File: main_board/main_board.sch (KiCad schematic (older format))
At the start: 132 parts, among them J1 stepper 0, J10 24VDCout5, J11 5VDCout0, J12 5VDCout1, J13 5VDCout2, J14 5VDCout3, J15 5VDCout4, J16 5VDCout5, J17 temperature measure 0, J18 temperature measure 1, J19 I2C, J2 stepper 1, J20 I2C, J21 I2C, J22 I2C, J23 hall measure 0, J24 weight measure 0, J25 light measure 0, J26 24VDC_in, J27 24VDC to 5VDC step down, J28 24VDC, J29 24VDC, J3 stepper 2, J30 24VDC, J31 5VDC, J32 5VDC, J33 5VDC, J34 hall measure 1, J35 reflective sensor 0, J36 24VDC, J37 24VDC, J38 24VDC, J39 5VDC, J4 stepper 3, J40 5VDC, J41 5VDC, J42 Conn_01x05_Male, J5 24VDCout0, J6 24VDCout1, J7 24VDCout2, J8 24VDCout3, J9 24VDCout4, Q1 Q_NMOS_GDS, Q10 BS170, Q11 BS170, Q12 BS170, Q2 Q_NMOS_GDS, Q3 Q_NMOS_GDS, Q4 Q_NMOS_GDS, Q5 Q_NMOS_GDS, Q6 Q_NMOS_GDS, Q7 BS170, Q8 BS170, Q9 BS170, U1 ESP32-DEVKITC-32D, U2 PCA9685PW

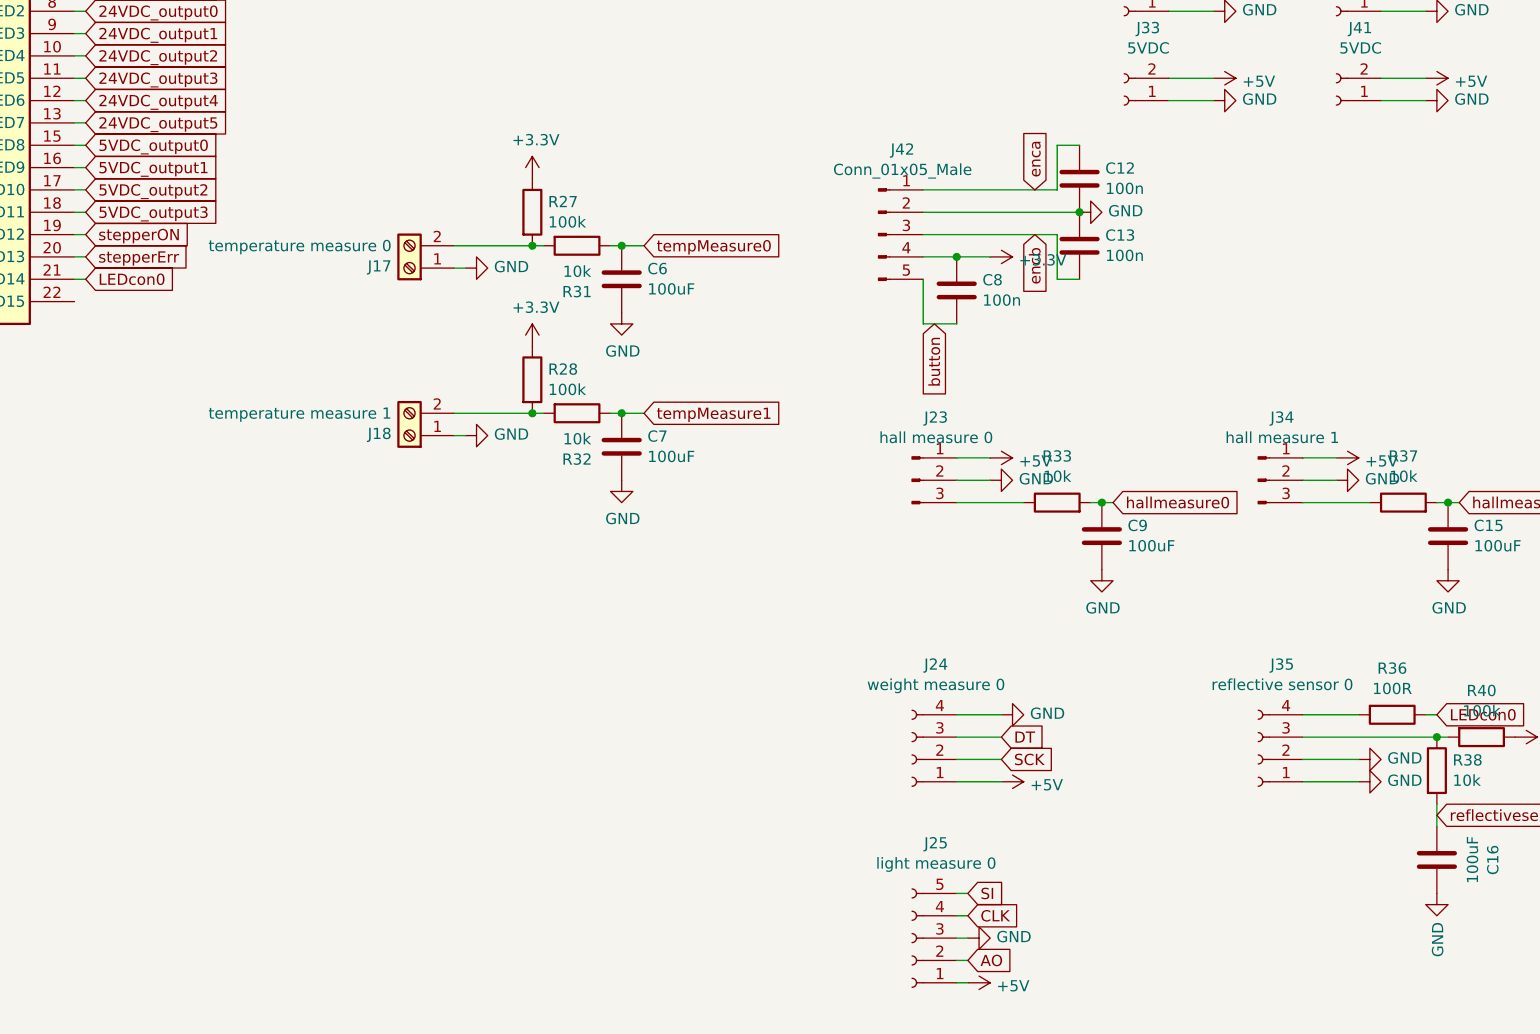
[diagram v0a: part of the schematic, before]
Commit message: added gnd zones
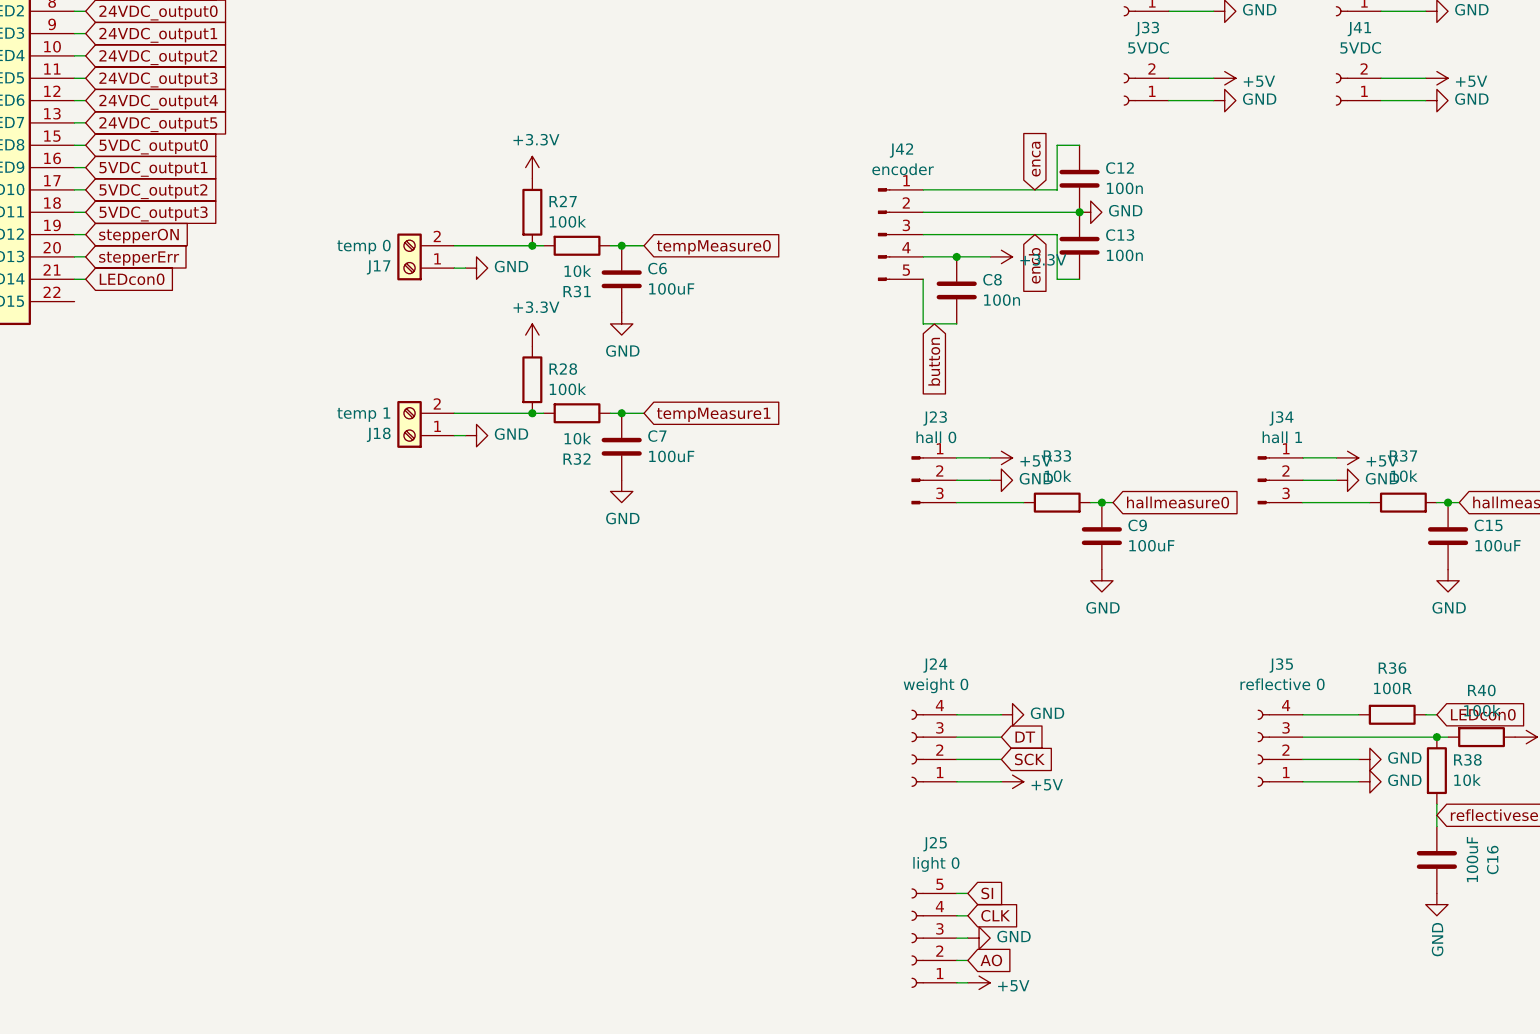
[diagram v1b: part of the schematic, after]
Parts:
- J17: value temperature measure 0 -> temp 0
- J18: value temperature measure 1 -> temp 1
- J23: value hall measure 0 -> hall 0
- J24: value weight measure 0 -> weight 0
- J25: value light measure 0 -> light 0
- J34: value hall measure 1 -> hall 1
- J35: value reflective sensor 0 -> reflective 0
- J42: value Conn_01x05_Male -> encoder

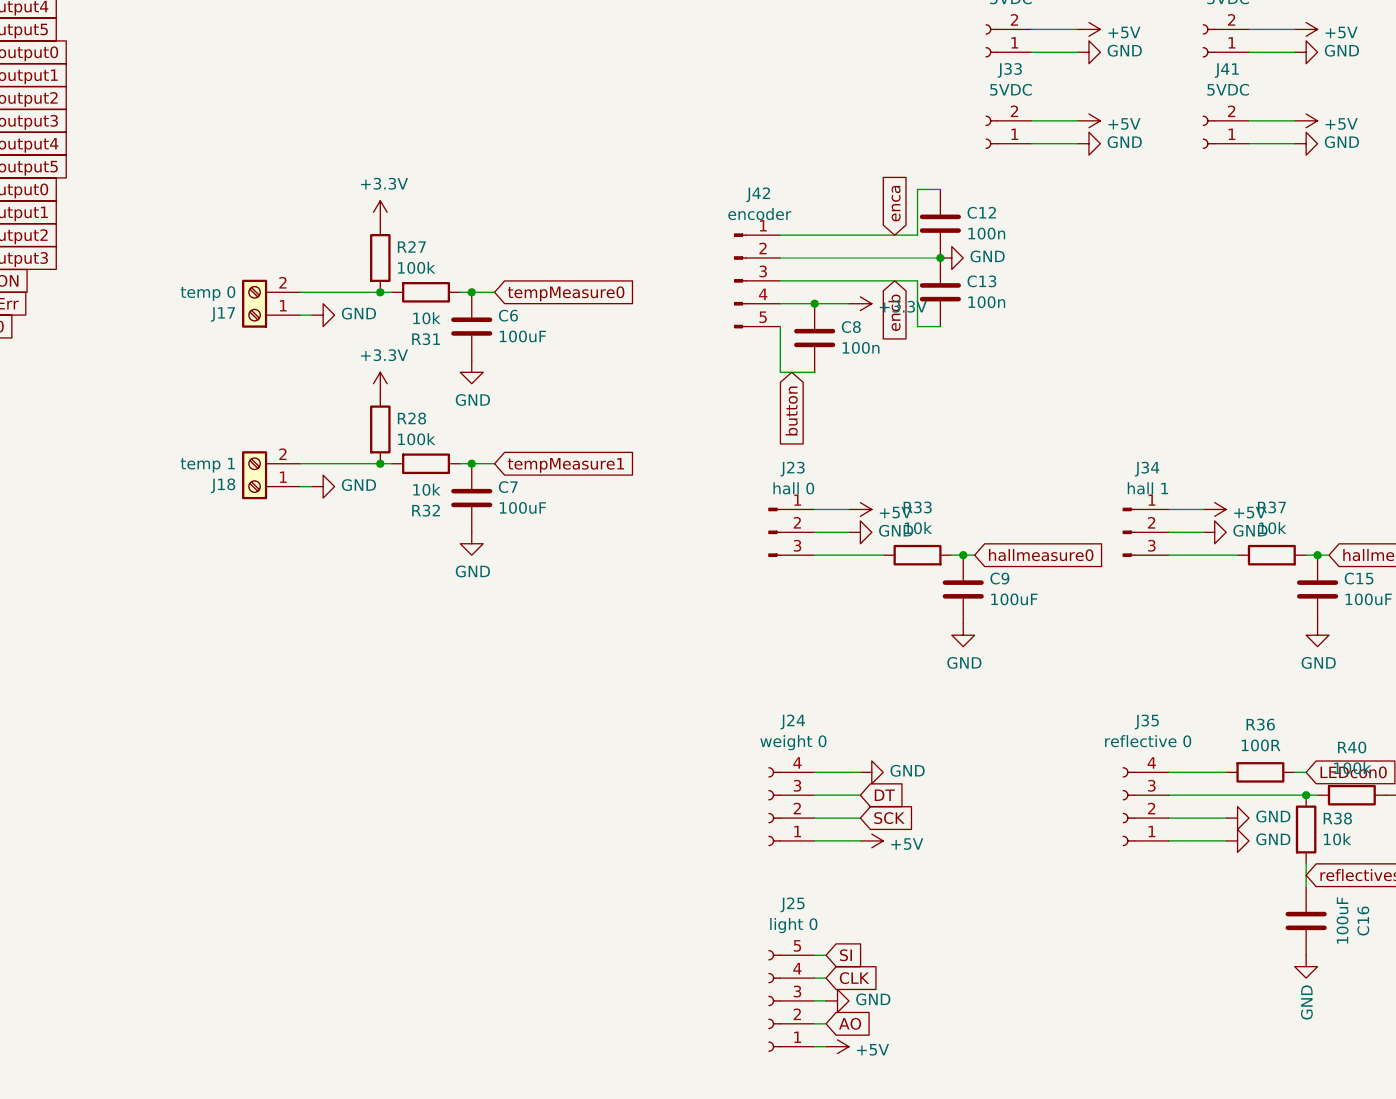
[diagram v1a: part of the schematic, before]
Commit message: part numbers added
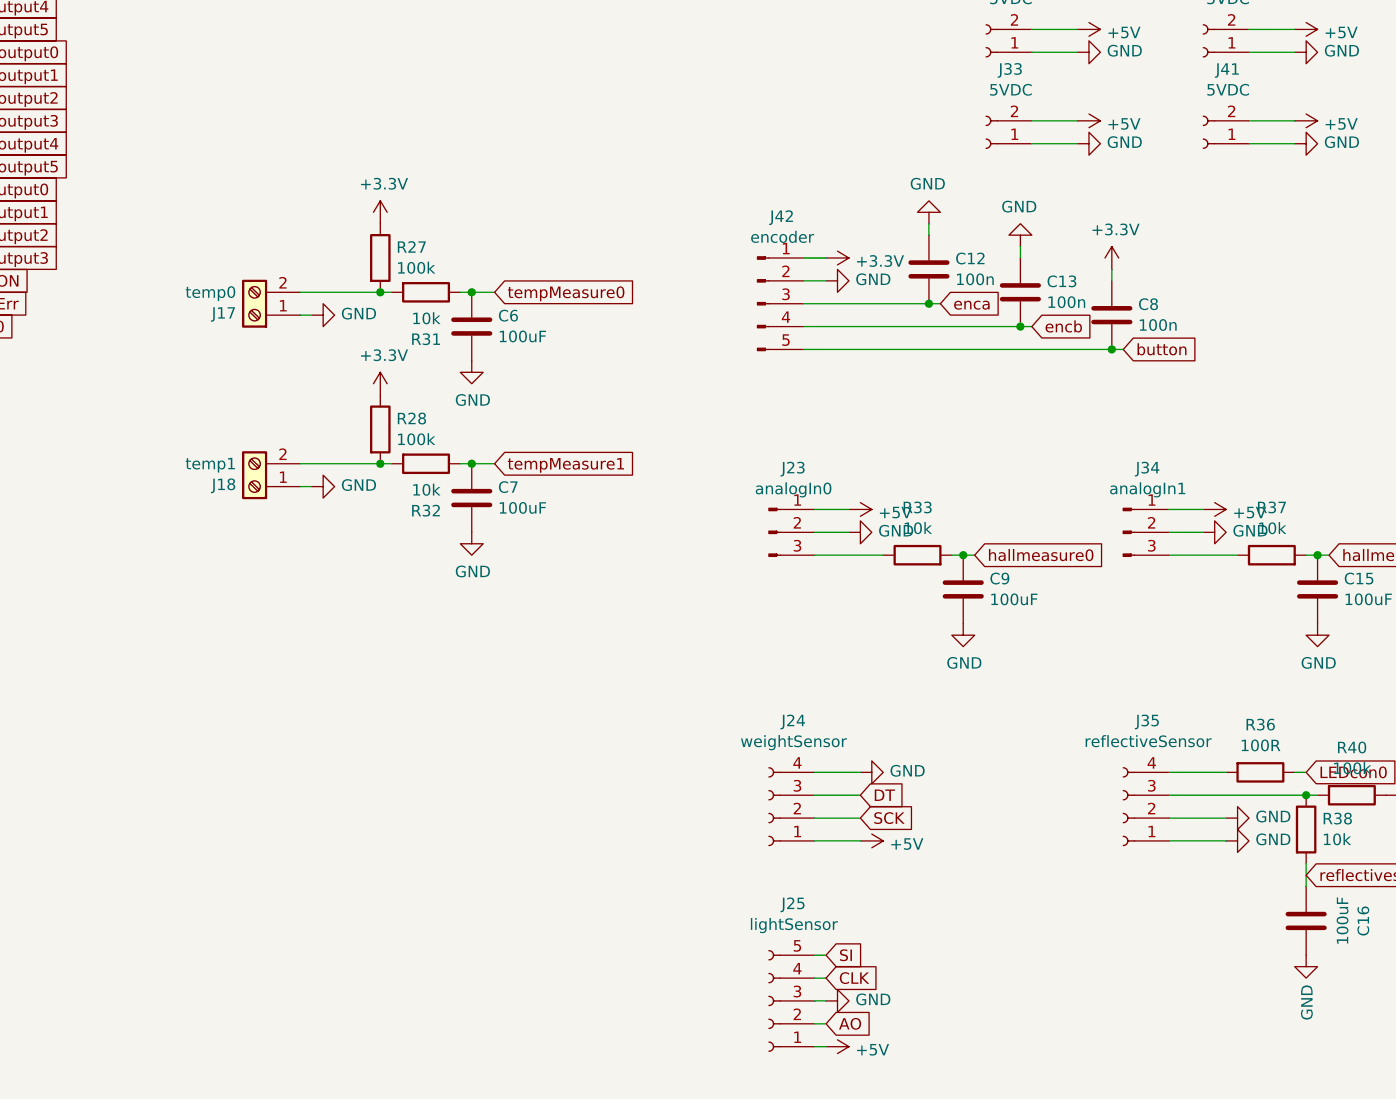
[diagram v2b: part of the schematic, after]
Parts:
- J17: value temp 0 -> temp0
- J18: value temp 1 -> temp1
- J23: value hall 0 -> analogIn0
- J24: value weight 0 -> weightSensor
- J25: value light 0 -> lightSensor
- J34: value hall 1 -> analogIn1
- J35: value reflective 0 -> reflectiveSensor
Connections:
- net +3V3: now also J42.1 (Pin_1); no longer J42.4 (Pin_4)
- net GND: now also C12.2; no longer C12.1
- net enca: now also C12.1, J42.3 (Pin_3); no longer C12.2, J42.1 (Pin_1)
- net encb: now also J42.4 (Pin_4); no longer J42.3 (Pin_3)
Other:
- moved on the sheet: C12, C13, C8, J42
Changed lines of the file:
@@
 Wire Wire Line
 	15000 2550 15200 2550
-Text GLabel 13450 4400 1    50   Input ~ 0
+Text GLabel 13650 4700 2    50   Input ~ 0
 enca
-Text GLabel 13450 4600 3    50   Input ~ 0
+Text GLabel 14050 4800 2    50   Input ~ 0
 encb
-Text GLabel 13000 5000 3    50   Input ~ 0
+Text GLabel 14450 4900 2    50   Input ~ 0
 button
 Text GLabel 9200 4100 2    50   Input ~ 0
@@
 P 12900 5700
 F 0 "J23" H 13008 5981 50  0000 C CNN
-F 1 "hall 0" H 13008 5890 50  0000 C CNN
+F 1 "analogIn0" H 13008 5890 50  0000 C CNN
 F 2 "Connector_PinHeader_2.54mm:PinHeader_1x03_P2.54mm_Vertical" H 12900 5700 50  0001 C CNN
 F 3 "~" H 12900 5700 50  0001 C CNN
@@
 L Device:C C8
 U 1 1 61B1A5D9
-P 13100 4850
-F 0 "C8" H 12985 4804 50  0000 R CNN
-F 1 "100n" H 12985 4895 50  0000 R CNN
-F 2 "Capacitor_SMD:C_0603_1608Metric_Pad1.08x0.95mm_HandSolder" H 13138 4700 50  0001 C CNN
-F 3 "~" H 13100 4850 50  0001 C CNN
-	1    13100 4850
+P 14400 4750
+F 0 "C8" H 14285 4704 50  0000 R CNN
+F 1 "100n" H 14285 4795 50  0000 R CNN
+F 2 "Capacitor_SMD:C_0603_1608Metric_Pad1.08x0.95mm_HandSolder" H 14438 4600 50  0001 C CNN
+F 3 "~" H 14400 4750 50  0001 C CNN
+	1    14400 4750
 	-1   0    0    1
 $EndComp
@@
 L Device:C C13
 U 1 1 61BB01E8
-P 13650 4650
-F 0 "C13" H 13535 4604 50  0000 R CNN
-F 1 "100n" H 13535 4695 50  0000 R CNN
-F 2 "Capacitor_SMD:C_0603_1608Metric_Pad1.08x0.95mm_HandSolder" H 13688 4500 50  0001 C CNN
-F 3 "~" H 13650 4650 50  0001 C CNN
-	1    13650 4650
+P 14000 4650
+F 0 "C13" H 13885 4604 50  0000 R CNN
+F 1 "100n" H 13885 4695 50  0000 R CNN
+F 2 "Capacitor_SMD:C_0603_1608Metric_Pad1.08x0.95mm_HandSolder" H 14038 4500 50  0001 C CNN
+F 3 "~" H 14000 4650 50  0001 C CNN
+	1    14000 4650
 	-1   0    0    1
 $EndComp
@@
 L Device:C C12
 U 1 1 61BC5069
-P 13650 4350
-F 0 "C12" H 13535 4304 50  0000 R CNN
-F 1 "100n" H 13535 4395 50  0000 R CNN
-F 2 "Capacitor_SMD:C_0603_1608Metric_Pad1.08x0.95mm_HandSolder" H 13688 4200 50  0001 C CNN
-F 3 "~" H 13650 4350 50  0001 C CNN
-	1    13650 4350
+P 13600 4550
+F 0 "C12" H 13485 4504 50  0000 R CNN
+F 1 "100n" H 13485 4595 50  0000 R CNN
+F 2 "Capacitor_SMD:C_0603_1608Metric_Pad1.08x0.95mm_HandSolder" H 13638 4400 50  0001 C CNN
+F 3 "~" H 13600 4550 50  0001 C CNN
+	1    13600 4550
 	-1   0    0    1
 $EndComp
@@
 P 10650 4750
 F 0 "J17" H 10730 4742 50  0000 L CNN
-F 1 "temp 0" H 10730 4651 50  0000 L CNN
+F 1 "temp0" H 10730 4651 50  0000 L CNN
 F 2 "TerminalBlock:TerminalBlock_bornier-2_P5.08mm" H 10650 4750 50  0001 C CNN
 F 3 "~" H 10650 4750 50  0001 C CNN
@@
 P 10650 5500
 F 0 "J18" H 10730 5492 50  0000 L CNN
-F 1 "temp 1" H 10730 5401 50  0000 L CNN
+F 1 "temp1" H 10730 5401 50  0000 L CNN
 F 2 "TerminalBlock:TerminalBlock_bornier-2_P5.08mm" H 10650 5500 50  0001 C CNN
 F 3 "~" H 10650 5500 50  0001 C CNN
@@
 L Connector:Conn_01x05_Male J42
 U 1 1 61FA40BF
-P 12750 4600
-F 0 "J42" H 12858 4981 50  0000 C CNN
-F 1 "encoder" H 12858 4890 50  0000 C CNN
-F 2 "Connector_PinHeader_2.54mm:PinHeader_1x05_P2.54mm_Vertical" H 12750 4600 50  0001 C CNN
-F 3 "~" H 12750 4600 50  0001 C CNN
-	1    12750 4600
+P 12850 4700
+F 0 "J42" H 12958 5081 50  0000 C CNN
+F 1 "encoder" H 12958 4990 50  0000 C CNN
+F 2 "Connector_PinHeader_2.54mm:PinHeader_1x05_P2.54mm_Vertical" H 12850 4700 50  0001 C CNN
+F 3 "~" H 12850 4700 50  0001 C CNN
+	1    12850 4700
 	1    0    0    -1
 $EndComp
@@
 L power:GND #PWR068
 U 1 1 61FA6407
-P 13650 4500
-F 0 "#PWR068" H 13650 4250 50  0001 C CNN
-F 1 "GND" V 13655 4372 50  0000 R CNN
-F 2 "" H 13650 4500 50  0001 C CNN
-F 3 "" H 13650 4500 50  0001 C CNN
-	1    13650 4500
+P 13150 4600
+F 0 "#PWR068" H 13150 4350 50  0001 C CNN
+F 1 "GND" V 13155 4472 50  0000 R CNN
+F 2 "" H 13150 4600 50  0001 C CNN
+F 3 "" H 13150 4600 50  0001 C CNN
+	1    13150 4600
 	0    -1   -1   0
 $EndComp
-Connection ~ 13650 4500
-Wire Wire Line
-	13650 4500 12950 4500
-Wire Wire Line
-	13550 4800 13550 4600
-Wire Wire Line
-	13550 4600 12950 4600
-Wire Wire Line
-	13550 4200 13550 4400
-Wire Wire Line
-	13550 4400 12950 4400
 $Comp
 L power:+3.3V #PWR058
 U 1 1 6243C181
-P 13250 4700
-F 0 "#PWR058" H 13250 4550 50  0001 C CNN
-F 1 "+3.3V" V 13265 4828 50  0000 L CNN
-F 2 "" H 13250 4700 50  0001 C CNN
-F 3 "" H 13250 4700 50  0001 C CNN
-	1    13250 4700
+P 13150 4500
+F 0 "#PWR058" H 13150 4350 50  0001 C CNN
+F 1 "+3.3V" V 13165 4628 50  0000 L CNN
+F 2 "" H 13150 4500 50  0001 C CNN
+F 3 "" H 13150 4500 50  0001 C CNN
+	1    13150 4500
 	0    1    1    0
 $EndComp
-Wire Wire Line
-	13250 4700 13100 4700
-Connection ~ 13100 4700
-Wire Wire Line
-	13100 4700 12950 4700
-Wire Wire Line
-	13100 5000 12950 5000
-Wire Wire Line
-	12950 5000 12950 4800
-Wire Wire Line
-	13550 4800 13650 4800
-Wire Wire Line
-	13550 4200 13650 4200
 $Comp
 L Mechanical:MountingHole H1
@@
 P 14450 5700
 F 0 "J34" H 14558 5981 50  0000 C CNN
-F 1 "hall 1" H 14558 5890 50  0000 C CNN
+F 1 "analogIn1" H 14558 5890 50  0000 C CNN
 F 2 "Connector_PinHeader_2.54mm:PinHeader_1x03_P2.54mm_Vertical" H 14450 5700 50  0001 C CNN
 F 3 "~" H 14450 5700 50  0001 C CNN
@@
 P 12900 6950
 F 0 "J24" H 12792 6525 50  0000 C CNN
-F 1 "weight 0" H 12792 6616 50  0000 C CNN
+F 1 "weightSensor" H 12792 6616 50  0000 C CNN
 F 2 "Connector_PinHeader_2.54mm:PinHeader_1x04_P2.54mm_Vertical" H 12900 6950 50  0001 C CNN
 F 3 "~" H 12900 6950 50  0001 C CNN
@@
 P 14450 6950
 F 0 "J35" H 14342 6525 50  0000 C CNN
-F 1 "reflective 0" H 14342 6616 50  0000 C CNN
+F 1 "reflectiveSensor" H 14342 6616 50  0000 C CNN
 F 2 "Connector_PinHeader_2.54mm:PinHeader_1x04_P2.54mm_Vertical" H 14450 6950 50  0001 C CNN
 F 3 "~" H 14450 6950 50  0001 C CNN
@@
 P 12900 7750
 F 0 "J25" H 12792 7325 50  0000 C CNN
-F 1 "light 0" H 12792 7416 50  0000 C CNN
+F 1 "lightSensor" H 12792 7416 50  0000 C CNN
 F 2 "Connector_PinHeader_2.54mm:PinHeader_1x05_P2.54mm_Vertical" H 12900 7750 50  0001 C CNN
 F 3 "~" H 12900 7750 50  0001 C CNN
@@
 	1    0    0    -1
 $EndComp
+Wire Wire Line
+	13150 4500 13050 4500
+Wire Wire Line
+	13150 4600 13050 4600
+Wire Wire Line
+	13650 4700 13600 4700
+Wire Wire Line
+	13600 4700 13050 4700
+Connection ~ 13600 4700
+Wire Wire Line
+	14050 4800 14000 4800
+Wire Wire Line
+	13050 4800 14000 4800
+Connection ~ 14000 4800
+Wire Wire Line
+	14450 4900 14400 4900
+Wire Wire Line
+	13050 4900 14400 4900
+Connection ~ 14400 4900
+$Comp
+L power:GND #PWR0110
+U 1 1 6205BD45
+P 13600 4350
+F 0 "#PWR0110" H 13600 4100 50  0001 C CNN
+F 1 "GND" H 13605 4177 50  0000 C CNN
+F 2 "" H 13600 4350 50  0001 C CNN
+F 3 "" H 13600 4350 50  0001 C CNN
+	1    13600 4350
+	-1   0    0    1
+$EndComp
+Wire Wire Line
+	13600 4400 13600 4350
+Wire Wire Line
+	14000 4500 14000 4450
+$Comp
+L power:+3.3V #PWR0112
+U 1 1 620E3D40
+P 14400 4550
+F 0 "#PWR0112" H 14400 4400 50  0001 C CNN
+F 1 "+3.3V" H 14415 4723 50  0000 C CNN
+F 2 "" H 14400 4550 50  0001 C CNN
+F 3 "" H 14400 4550 50  0001 C CNN
+	1    14400 4550
+	1    0    0    -1
+$EndComp
+Wire Wire Line
+	14400 4600 14400 4550
+$Comp
+L power:GND #PWR?
+U 1 1 6212881C
+P 14000 4450
+F 0 "#PWR?" H 14000 4200 50  0001 C CNN
+F 1 "GND" H 14005 4277 50  0000 C CNN
+F 2 "" H 14000 4450 50  0001 C CNN
+F 3 "" H 14000 4450 50  0001 C CNN
+	1    14000 4450
+	-1   0    0    1
+$EndComp
 $EndSCHEMATC
